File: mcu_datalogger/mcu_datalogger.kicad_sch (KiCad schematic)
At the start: 25 parts, among them U1 24LC1025, U2 24LC1025, U3 DS1337S_, U4 ATMEGA328P-AU, Y1 Crystal, Y2 Crystal

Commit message: add values
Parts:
- C1, C4: value C -> 0.1uF
- C2, C3: value C -> 22pF
- C5: value C_Polarized -> 100nF
- R1, R6: value R -> 4.7K
- R2, R3, R7: value R -> 10K
- R4, R5: value R -> 330
- Y1: value Crystal -> 32.768 KHz
- Y2: value Crystal -> 16 MHz
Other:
- moved on the sheet: C5, R7, Y1
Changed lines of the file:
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@@
 			)
 		)
-		(property "Value" "C"
+		(property "Value" "22pF"
 			(at 168.91 63.4999 0)
 			(show_name no)
@@
 			)
 		)
-		(property "Value" "C"
+		(property "Value" "22pF"
 			(at 168.91 78.7399 0)
 			(show_name no)
@@
 			)
 		)
-		(property "Value" "R"
+		(property "Value" "4.7K"
 			(at 101.6 161.2899 0)
 			(show_name no)
@@
 			)
 		)
-		(property "Value" "R"
+		(property "Value" "330"
 			(at 243.84 74.9299 0)
 			(show_name no)
@@
 			)
 		)
-		(property "Value" "Crystal"
+		(property "Value" "16 MHz"
 			(at 184.15 64.7699 90)
 			(show_name no)
@@
 			)
 		)
-		(property "Value" "R"
+		(property "Value" "10K"
 			(at 107.95 38.0999 0)
 			(show_name no)
@@
 			)
 		)
-		(property "Value" "C"
+		(property "Value" "0.1uF"
 			(at 180.34 27.94 90)
 			(show_name no)
@@
 			)
 		)
-		(property "Value" "C"
+		(property "Value" "0.1uF"
 			(at 123.19 38.0999 0)
 			(show_name no)
@@
 	(symbol
 		(lib_id "Device:Crystal")
-		(at 30.48 45.72 0)
+		(at 30.48 45.72 90)
 		(unit 1)
 		(body_style 1)
@@
 		(fields_autoplaced yes)
 		(property "Reference" "Y1"
-			(at 30.48 38.1 0)
-			(show_name no)
-			(do_not_autoplace no)
-			(effects
-				(font
-					(size 1.27 1.27)
-				)
-			)
-		)
-		(property "Value" "Crystal"
-			(at 30.48 40.64 0)
-			(show_name no)
-			(do_not_autoplace no)
-			(effects
-				(font
-					(size 1.27 1.27)
-				)
+			(at 34.29 44.4499 90)
+			(show_name no)
+			(do_not_autoplace no)
+			(effects
+				(font
+					(size 1.27 1.27)
+				)
+				(justify right)
+			)
+		)
+		(property "Value" "32.768 KHz"
+			(at 34.29 46.9899 90)
+			(show_name no)
+			(do_not_autoplace no)
+			(effects
+				(font
+					(size 1.27 1.27)
+				)
+				(justify right)
 			)
 		)
@@
 			)
 		)
-		(property "Value" "R"
+		(property "Value" "10K"
 			(at 95.25 38.0999 0)
 			(show_name no)
@@
 			)
 		)
-		(property "Value" "R"
+		(property "Value" "4.7K"
 			(at 90.17 161.2899 0)
 			(show_name no)
@@
 	(symbol
 		(lib_id "Device:C_Polarized")
-		(at 250.19 39.37 0)
+		(at 247.65 39.37 0)
 		(unit 1)
 		(body_style 1)
@@
 		(fields_autoplaced yes)
 		(property "Reference" "C5"
-			(at 254 37.2109 0)
-			(show_name no)
-			(do_not_autoplace no)
-			(effects
-				(font
-					(size 1.27 1.27)
-				)
-				(justify left)
-			)
-		)
-		(property "Value" "C_Polarized"
-			(at 254 39.7509 0)
+			(at 251.46 37.2109 0)
+			(show_name no)
+			(do_not_autoplace no)
+			(effects
+				(font
+					(size 1.27 1.27)
+				)
+				(justify left)
+			)
+		)
+		(property "Value" "100nF"
+			(at 251.46 39.7509 0)
 			(show_name no)
 			(do_not_autoplace no)
@@
 		)
 		(property "Footprint" ""
-			(at 251.1552 43.18 0)
+			(at 248.6152 43.18 0)
 			(hide yes)
 			(show_name no)
@@
 		)
 		(property "Datasheet" ""
-			(at 250.19 39.37 0)
+			(at 247.65 39.37 0)
 			(hide yes)
 			(show_name no)
@@
 		)
 		(property "Description" "Polarized capacitor"
-			(at 250.19 39.37 0)
+			(at 247.65 39.37 0)
 			(hide yes)
 			(show_name no)
@@
 	(symbol
 		(lib_id "Device:R")
-		(at 184.15 91.44 90)
+		(at 182.88 86.36 90)
 		(unit 1)
 		(body_style 1)
@@
 		(fields_autoplaced yes)
 		(property "Reference" "R7"
-			(at 184.15 85.09 90)
-			(show_name no)
-			(do_not_autoplace no)
-			(effects
-				(font
-					(size 1.27 1.27)
-				)
-			)
-		)
-		(property "Value" "R"
-			(at 184.15 87.63 90)
+			(at 182.88 80.01 90)
+			(show_name no)
+			(do_not_autoplace no)
+			(effects
+				(font
+					(size 1.27 1.27)
+				)
+			)
+		)
+		(property "Value" "10K"
+			(at 182.88 82.55 90)
 			(show_name no)
 			(do_not_autoplace no)
@@
 		)
 		(property "Footprint" ""
-			(at 184.15 93.218 90)
+			(at 182.88 88.138 90)
 			(hide yes)
 			(show_name no)
@@
 		)
 		(property "Datasheet" ""
-			(at 184.15 91.44 0)
+			(at 182.88 86.36 0)
 			(hide yes)
 			(show_name no)
@@
 		)
 		(property "Description" "Resistor"
-			(at 184.15 91.44 0)
+			(at 182.88 86.36 0)
 			(hide yes)
 			(show_name no)
@@
 			)
 		)
-		(property "Value" "R"
+		(property "Value" "330"
 			(at 165.1 44.45 90)
 			(show_name no)

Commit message: assign footprints
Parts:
- BT1: footprint (none) -> Connector_PinHeader_2.54mm:PinHeader_1x02_P2.54mm_Vertical
- C1, C2, C3, C4, C5: footprint (none) -> Capacitor_SMD:C_0805_2012Metric
- D1, D2: footprint (none) -> LED_SMD:LED_0805_2012Metric
- H1, H2, H3, H4: footprint (none) -> MountingHole:MountingHole_2.1mm
- R1, R2, R3, R4, R5, R6, R7: footprint (none) -> Resistor_SMD:R_0805_2012Metric
- U1, U2: footprint (none) -> Package_SO:SOIC-8_3.9x4.9mm_P1.27mm
- U3: footprint DS1337S_:SOIC127P600X175-8N -> Footprints:SOIC127P600X175-8N
- U4: footprint ATMEGA328P-AU:QFP80P900X900X120-32N -> Footprints:QFP80P900X900X120-32N
- Y1, Y2: footprint (none) -> Crystal:Crystal_SMD_5032-2Pin_5.0x3.2mm_HandSoldering
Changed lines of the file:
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@@
 			)
 		)
-		(property "Footprint" ""
+		(property "Footprint" "Capacitor_SMD:C_0805_2012Metric"
 			(at 166.0652 66.04 0)
 			(hide yes)
@@
 			)
 		)
-		(property "Footprint" ""
+		(property "Footprint" "LED_SMD:LED_0805_2012Metric"
 			(at 181.61 48.26 0)
 			(hide yes)
@@
 			)
 		)
-		(property "Footprint" ""
+		(property "Footprint" "LED_SMD:LED_0805_2012Metric"
 			(at 241.3 59.69 0)
 			(hide yes)
@@
 			)
 		)
-		(property "Footprint" ""
+		(property "Footprint" "Capacitor_SMD:C_0805_2012Metric"
 			(at 166.0652 81.28 0)
 			(hide yes)
@@
 			)
 		)
-		(property "Footprint" ""
+		(property "Footprint" "Resistor_SMD:R_0805_2012Metric"
 			(at 97.282 160.02 90)
 			(hide yes)
@@
 			)
 		)
-		(property "Footprint" ""
+		(property "Footprint" "Resistor_SMD:R_0805_2012Metric"
 			(at 239.522 73.66 90)
 			(hide yes)
@@
 			)
 		)
-		(property "Footprint" "ATMEGA328P-AU:QFP80P900X900X120-32N"
+		(property "Footprint" "Footprints:QFP80P900X900X120-32N"
 			(at 218.44 59.69 0)
 			(hide yes)
@@
 			)
 		)
-		(property "Footprint" ""
+		(property "Footprint" "MountingHole:MountingHole_2.1mm"
 			(at 247.65 140.97 0)
 			(hide yes)
@@
 			)
 		)
-		(property "Footprint" ""
+		(property "Footprint" "Crystal:Crystal_SMD_5032-2Pin_5.0x3.2mm_HandSoldering"
 			(at 180.34 63.5 0)
 			(hide yes)
@@
 			)
 		)
-		(property "Footprint" ""
+		(property "Footprint" "Package_SO:SOIC-8_3.9x4.9mm_P1.27mm"
 			(at 69.85 160.02 0)
 			(hide yes)
@@
 			)
 		)
-		(property "Footprint" ""
+		(property "Footprint" "Resistor_SMD:R_0805_2012Metric"
 			(at 103.632 36.83 90)
 			(hide yes)
@@
 			)
 		)
-		(property "Footprint" ""
+		(property "Footprint" "Capacitor_SMD:C_0805_2012Metric"
 			(at 176.53 33.9852 0)
 			(hide yes)
@@
 			)
 		)
-		(property "Footprint" ""
+		(property "Footprint" "Capacitor_SMD:C_0805_2012Metric"
 			(at 120.3452 40.64 0)
 			(hide yes)
@@
 			)
 		)
-		(property "Footprint" "DS1337S_:SOIC127P600X175-8N"
+		(property "Footprint" "Footprints:SOIC127P600X175-8N"
 			(at 63.5 46.99 0)
 			(hide yes)
@@
 			)
 		)
-		(property "Footprint" ""
+		(property "Footprint" "MountingHole:MountingHole_2.1mm"
 			(at 247.65 154.94 0)
 			(hide yes)
@@
 			)
 		)
-		(property "Footprint" ""
+		(property "Footprint" "Crystal:Crystal_SMD_5032-2Pin_5.0x3.2mm_HandSoldering"
 			(at 30.48 45.72 0)
 			(hide yes)
@@
 			)
 		)
-		(property "Footprint" ""
+		(property "Footprint" "Resistor_SMD:R_0805_2012Metric"
 			(at 90.932 36.83 90)
 			(hide yes)
@@
 			)
 		)
-		(property "Footprint" ""
+		(property "Footprint" "MountingHole:MountingHole_2.1mm"
 			(at 247.65 147.32 0)
 			(hide yes)
@@
 			)
 		)
-		(property "Footprint" ""
+		(property "Footprint" "Connector_PinHeader_2.54mm:PinHeader_1x02_P2.54mm_Vertical"
 			(at 270.51 37.846 90)
 			(hide yes)
@@
 			)
 		)
-		(property "Footprint" ""
+		(property "Footprint" "Resistor_SMD:R_0805_2012Metric"
 			(at 85.852 160.02 90)
 			(hide yes)
@@
 			)
 		)
-		(property "Footprint" ""
+		(property "Footprint" "Package_SO:SOIC-8_3.9x4.9mm_P1.27mm"
 			(at 41.91 160.02 0)
 			(hide yes)
@@
 			)
 		)
-		(property "Footprint" ""
+		(property "Footprint" "Capacitor_SMD:C_0805_2012Metric"
 			(at 248.6152 43.18 0)
 			(hide yes)
@@
 			)
 		)
-		(property "Footprint" ""
+		(property "Footprint" "Resistor_SMD:R_0805_2012Metric"
 			(at 182.88 88.138 90)
 			(hide yes)
@@
 			)
 		)
-		(property "Footprint" ""
+		(property "Footprint" "Resistor_SMD:R_0805_2012Metric"
 			(at 165.1 50.038 90)
 			(hide yes)
@@
 			)
 		)
-		(property "Footprint" ""
+		(property "Footprint" "MountingHole:MountingHole_2.1mm"
 			(at 247.65 133.35 0)
 			(hide yes)

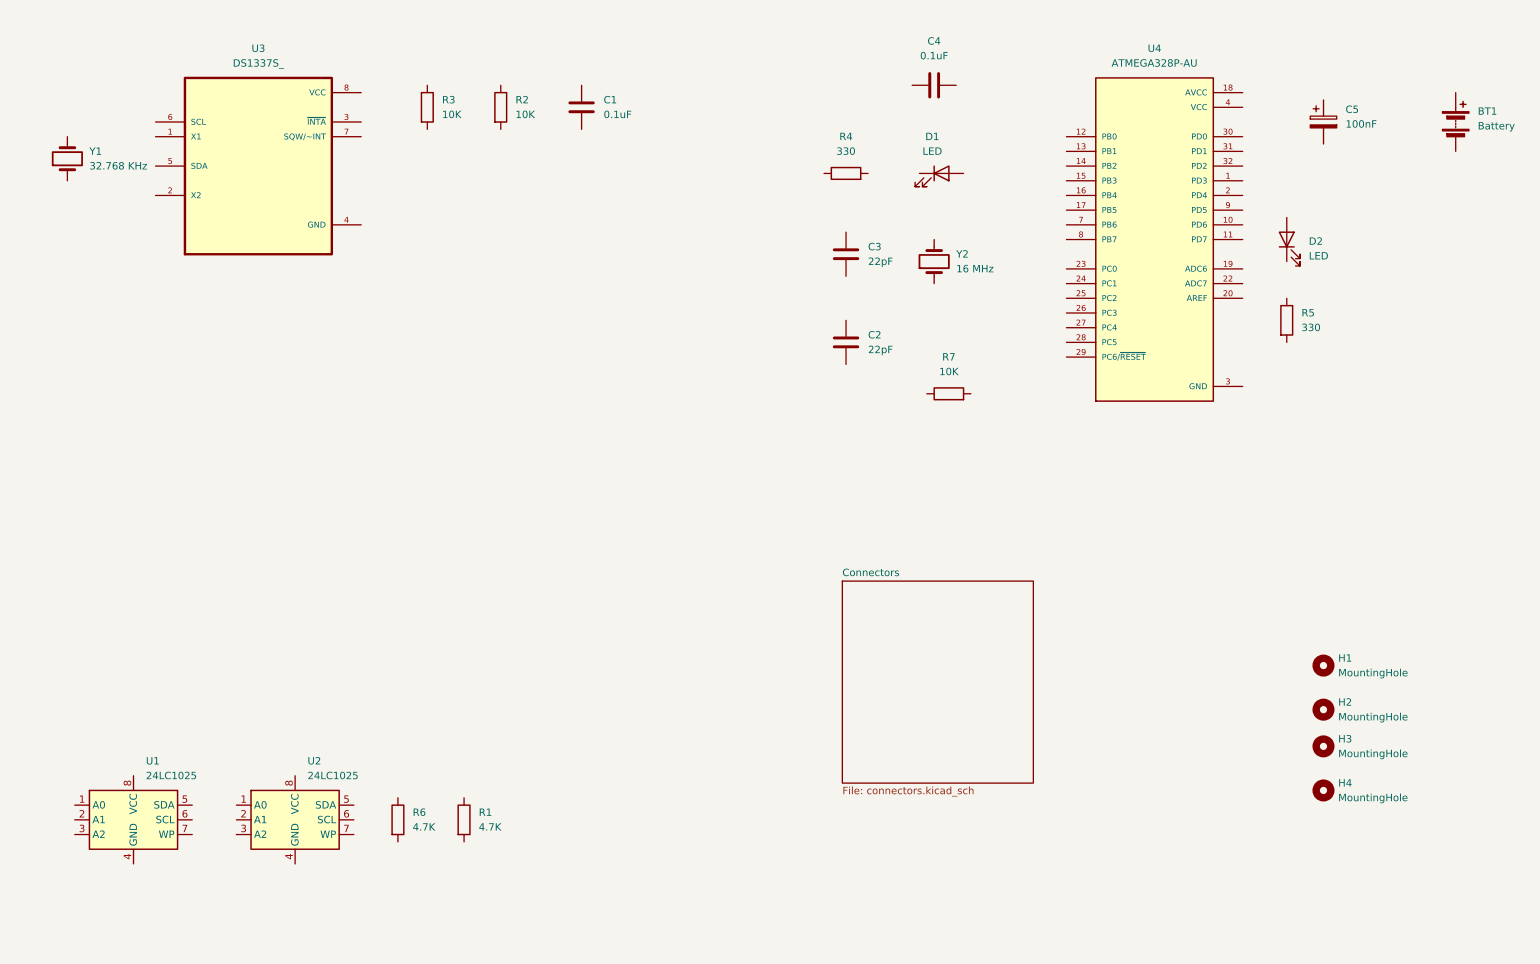
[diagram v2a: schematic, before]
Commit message: first scehmatic sheet wired
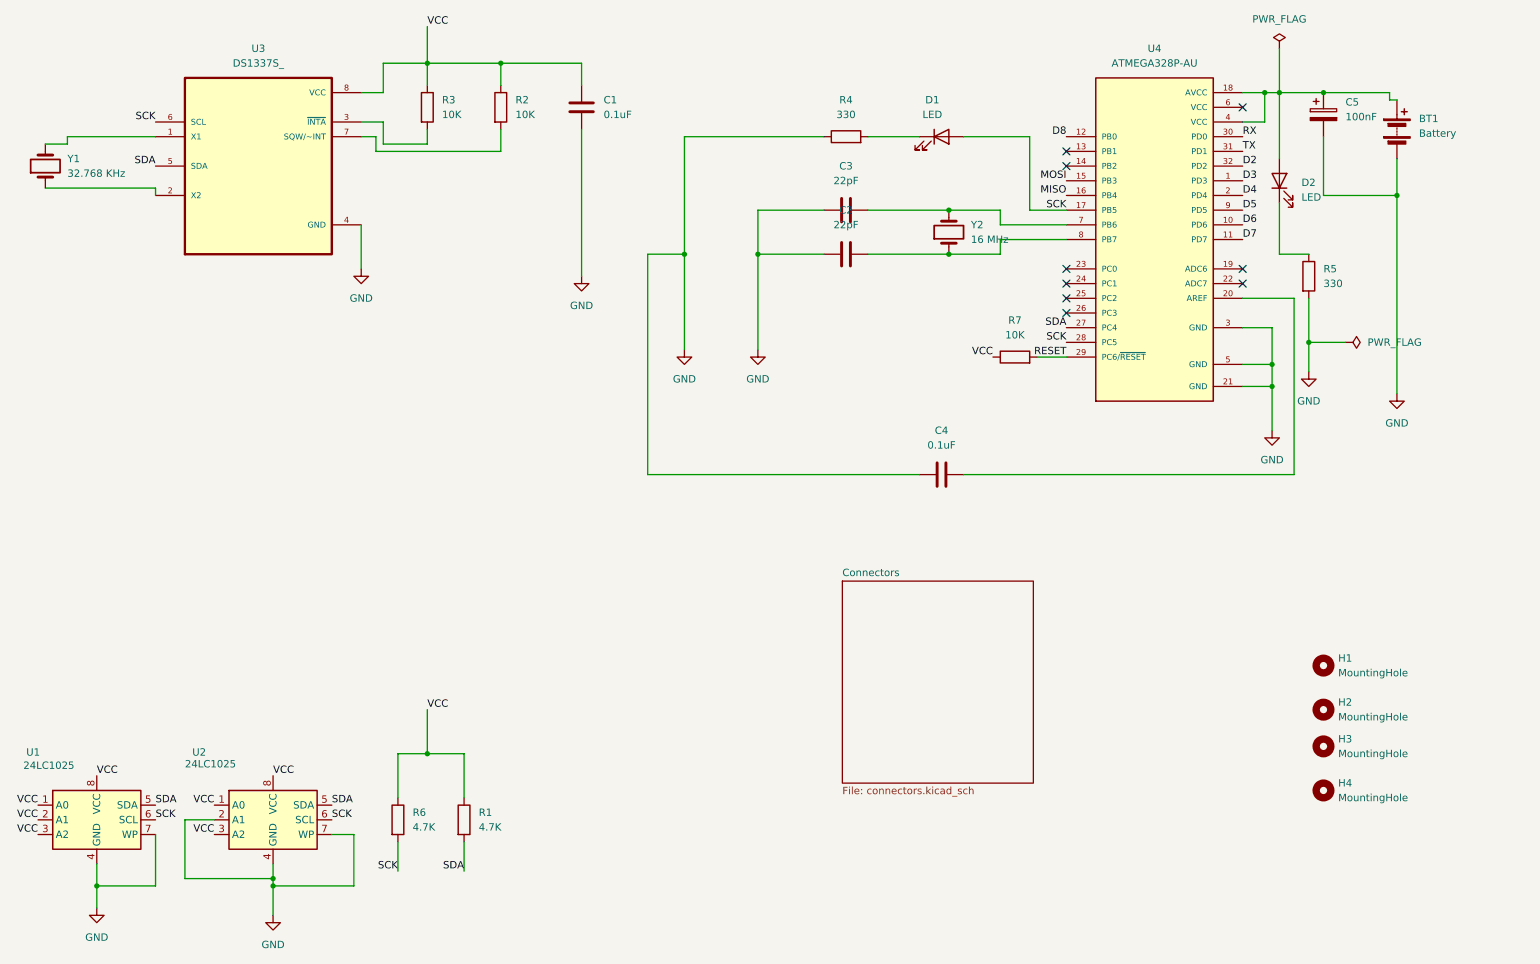
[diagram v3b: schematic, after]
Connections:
- net GND: now also BT1.2 (-), C1.2, C2.1, C3.1, C4.2, C5.2, R4.1, R5.2, U1.4 (GND), U1.7 (WP), U2.2 (A1), U2.4 (GND), U2.7 (WP), U3.4 (GND)
- net VCC: now also C1.1, R1.1, R2.1, R3.1, R6.1, R7.1, U1.1 (A0), U1.2 (A1), U1.3 (A2), U1.8 (VCC), U2.1 (A0), U2.3 (A2), U2.8 (VCC), U3.8 (VCC); no longer U4.4 (VCC), U4.6 (VCC)
- net at C3.2: now also U4.7 (PB6), Y2.2
- net at D1.1 (K): now also R4.2
- net SCK: now reaches D1.2 (A)
- net SCK: now also R6.2, U1.6 (SCL), U2.6 (SCL), U3.6 (SCL), U4.17 (PB5), U4.28 (PC5)
- net at D2.1 (K): now also R5.1
- net at D2.2 (A): now also BT1.1 (+), C5.1, U4.18 (AVCC), U4.4 (VCC)
- net at C2.2: now also U4.8 (PB7), Y2.1
- net SDA: now reaches R1.2
- net SDA: now also U1.5 (SDA), U2.5 (SDA), U3.5 (SDA), U4.27 (PC4)
- net D3: now reaches U4.1 (PD3)
- net D6: now reaches U4.10 (PD6)
- net D7: now reaches U4.11 (PD7)
- net D8: now reaches U4.12 (PB0)
- net MOSI: now reaches U4.15 (PB3)
- net MISO: now reaches U4.16 (PB4)
- net D4: now reaches U4.2 (PD4)
- net at U4.20 (AREF): now also C4.1
- net RESET: now reaches U4.29 (PC6/~{RESET})
- net RESET: now also R7.2
- net RX: now reaches U4.30 (PD0)
- net TX: now reaches U4.31 (PD1)
- net D2: now reaches U4.32 (PD2)
- net D5: now reaches U4.9 (PD5)
- net at R2.2: now also U3.7 (SQW/~INT)
- net at U3.1 (X1): now also Y1.2
- net at U3.2 (X2): now also Y1.1
- net at U3.3 (~{INTA}): now also R3.2
- no-connect marks 0 -> 9
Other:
- moved on the sheet: BT1, C2, C3, C4, C5, D1, D2, R4, R5, R7, U1, U2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
